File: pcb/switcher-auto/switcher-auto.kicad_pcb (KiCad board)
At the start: 4 copper layers, 160 x 110 mm, 42 parts, among them J1 MD-90SM, J10 MD-90SM, J11 MD-90SM, J12 MD-90SM, J13 MD-90SM, J14 MD-90SM, J15 Conn_02x22_Top_Bottom, J2 Conn_02x22_Top_Bottom, J3 Conn_02x22_Top_Bottom, J4 Conn_02x22_Top_Bottom, SW1 SW_Push, SW2 SW_Push, U1 CD74HC4067SM96, U2 CD74HC4067SM96, U3 CD74HC4067SM96, U4 CD74HC4067SM96, U5 CD74HC4067SM96, U6 CD74HC4067SM96, U7 CD74HC4067SM96

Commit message: Add notes for fab
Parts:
- added H5: MountingHole, MountingHole:MountingHole_2.5mm, F.Cu at (75.0, 37.0)
- renumbered H1 to H10, H2 to H12, H3 to H13, H4 to H14
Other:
- board size 160 x 110 mm -> 160 x 109 mm
- board text added: "PANEL A"
- board text added: "PANEL B"

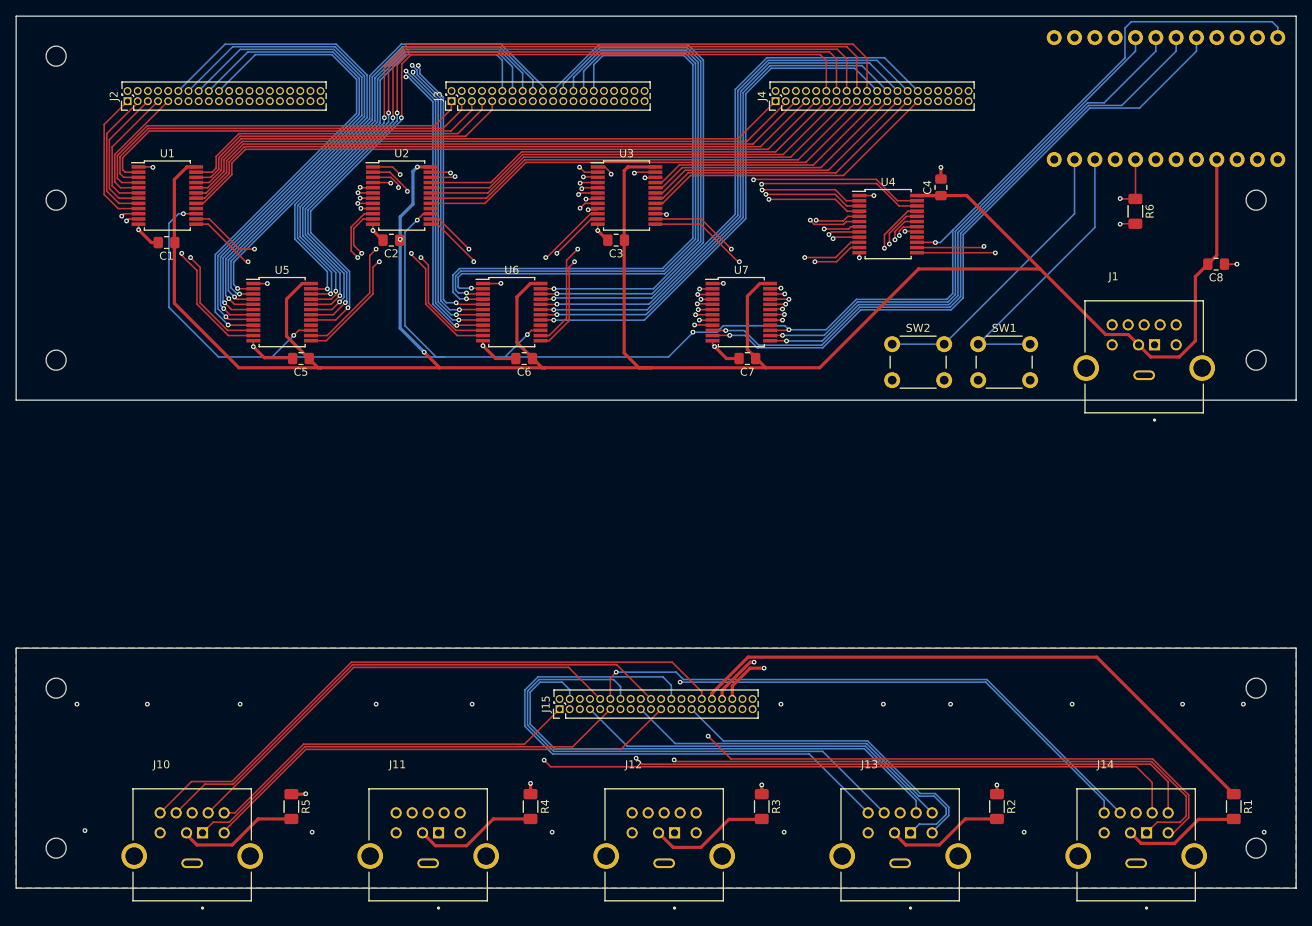
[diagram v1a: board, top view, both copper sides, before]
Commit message: mounting holes should be M3
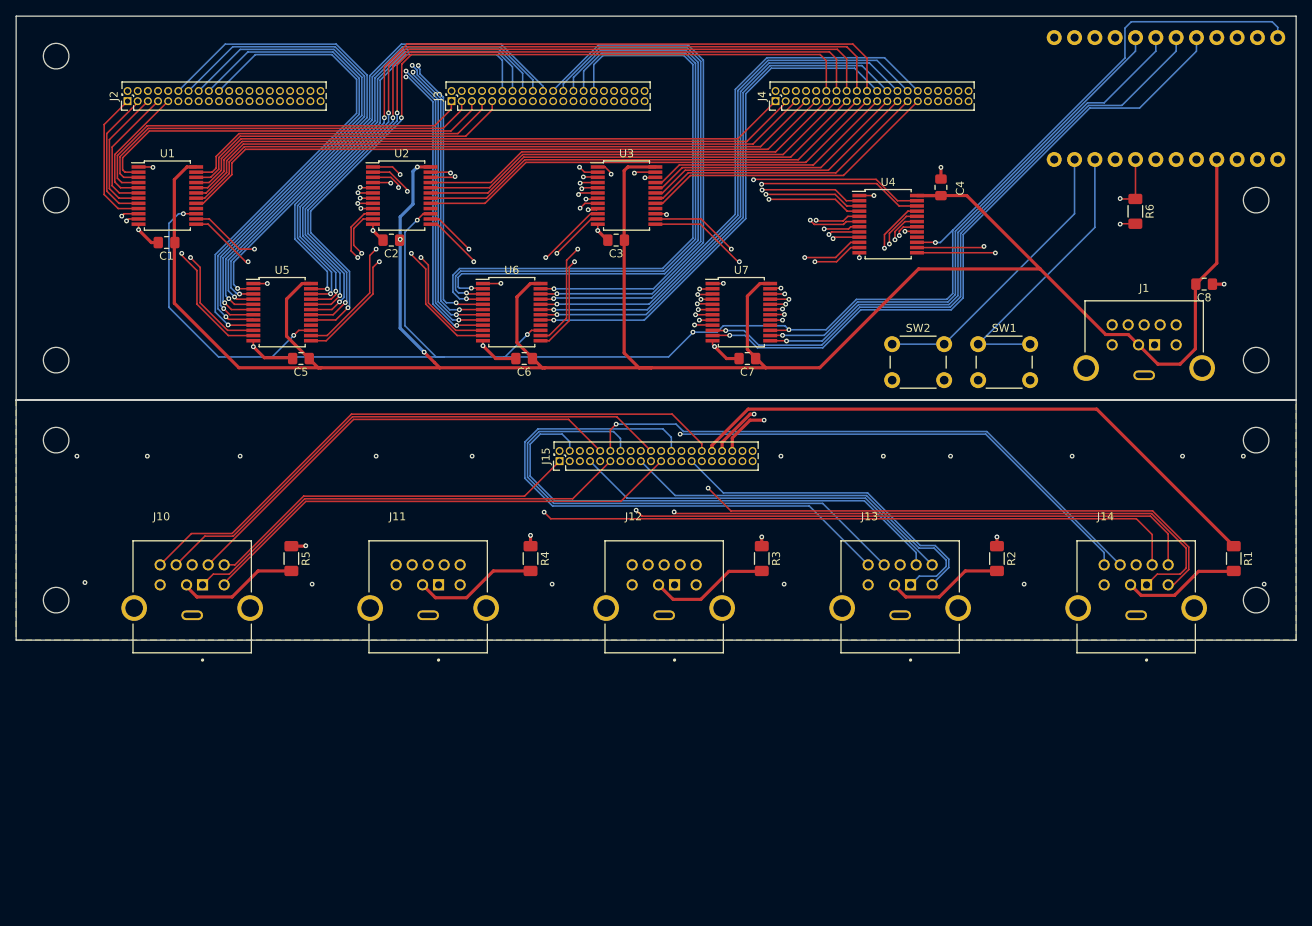
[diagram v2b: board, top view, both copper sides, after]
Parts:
- H1, H10, H12, H13, H14, H2, H3, H4, H5: footprint MountingHole:MountingHole_2.5mm -> MountingHole:MountingHole_3.2mm_M3
- moved R1 31.0 mm to (222.2, 99.8)
- moved R2 31.0 mm to (192.6, 99.8)
- moved R3 31.0 mm to (163.2, 99.8)
- moved R4 31.0 mm to (134.3, 99.8)
- moved R5 31.0 mm to (104.4, 99.8)
- moved H10 31.0 mm to (75.0, 85.0)
- moved H12 31.0 mm to (75.0, 105.0)
- moved H13 31.0 mm to (225.0, 85.0)
- moved H14 31.0 mm to (225.0, 105.0)
- moved J10 31.0 mm to (92.0, 106.9)
- moved J11 31.0 mm to (121.5, 106.9)
- moved J12 31.0 mm to (151.0, 106.9)
- moved J13 31.0 mm to (180.5, 106.9)
- moved J14 31.0 mm to (210.0, 106.9)
- moved J15 31.0 mm to (137.9, 87.6)
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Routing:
- net /VCC: track 309.0 -> 310.3 mm
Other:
- board size 160 x 109 mm -> 160 x 78 mm
- board text added: "DESIGN A"
- board text added: "DESIGN B"
- board text added: "V-Score or cut on this line"
- board text removed: "PANEL A"
- board text removed: "PANEL B"

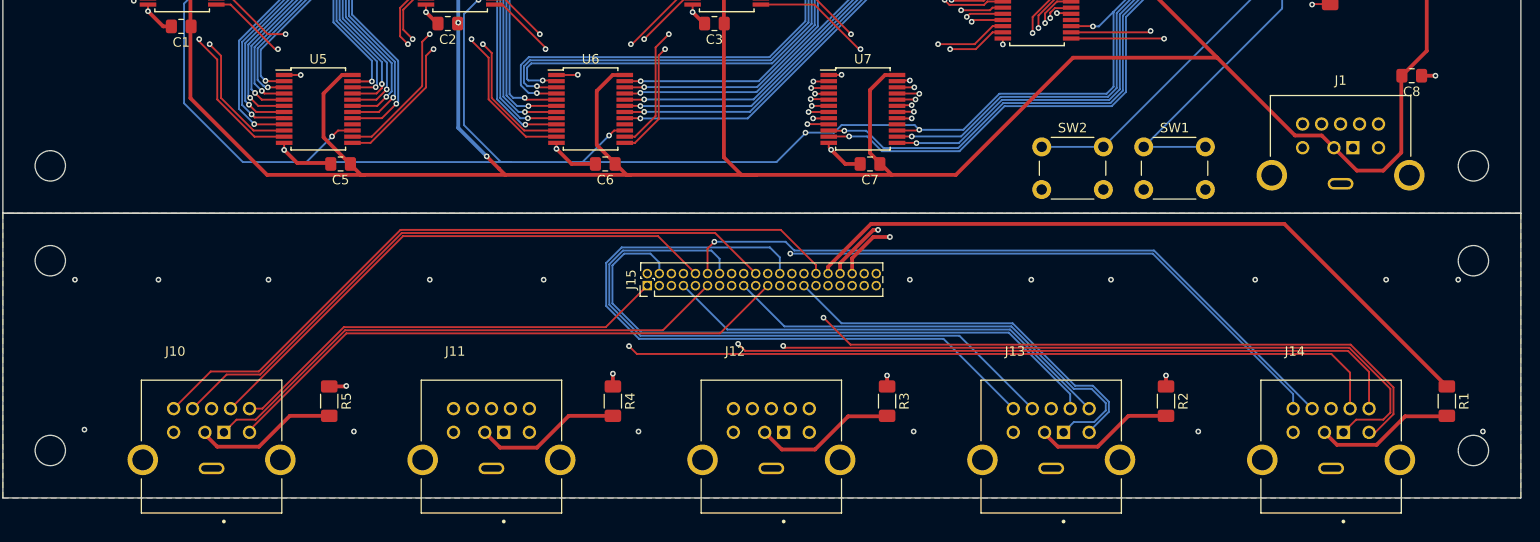
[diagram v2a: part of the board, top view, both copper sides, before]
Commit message: Remove silkscreens, passing DRC
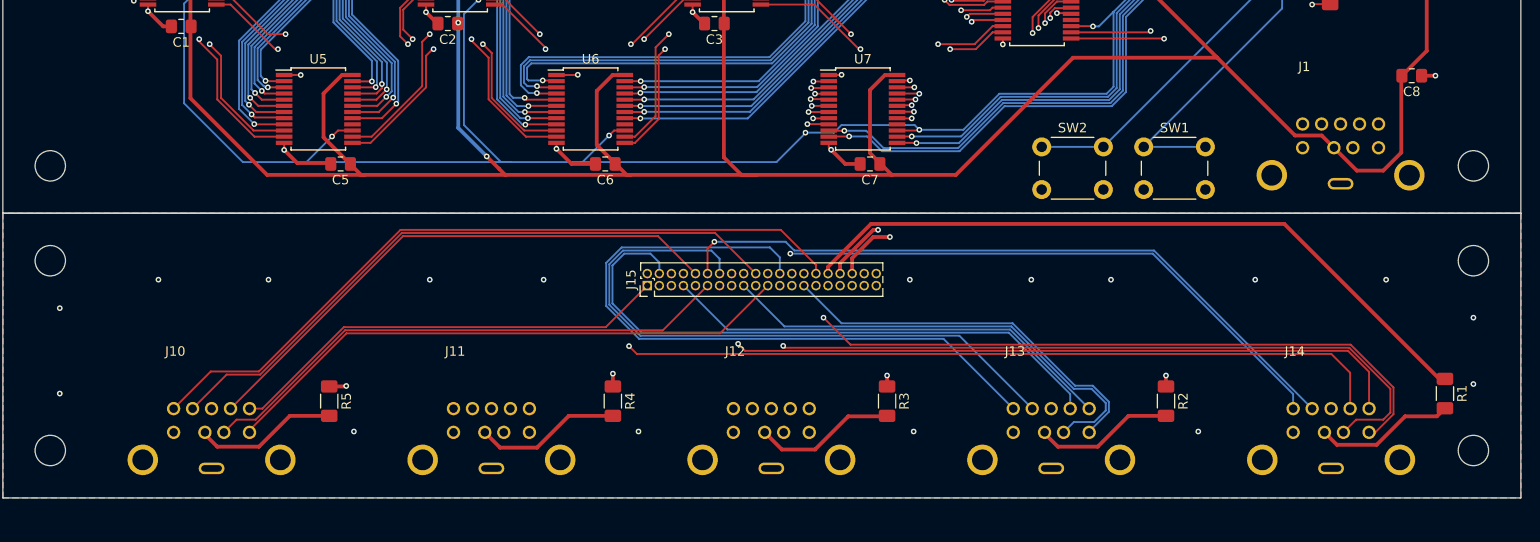
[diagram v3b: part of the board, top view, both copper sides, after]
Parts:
- moved R1 0.82 mm to (222.0, 99.0)
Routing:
- net Net-(J15-Pin_25): track 74.9 -> 74.4 mm

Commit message: WIP
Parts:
- R1, R2, R3, R4, R5, R6: footprint Resistor_SMD:R_1206_3216Metric_Pad1.30x1.75mm_HandSolder -> Resistor_SMD:R_0805_2012Metric_Pad1.20x1.40mm_HandSolder
- U1, U2, U3, U4, U5, U6, U7: footprint Package_SO:SSOP-24_5.3x8.2mm_P0.65mm -> Package_SO:SOIC-24W_7.5x15.4mm_P1.27mm
- moved H10 300.8 mm to (31.1, 382.6)
- moved H12 300.8 mm to (31.1, 402.6)
- moved H13 300.8 mm to (181.1, 382.6)
- moved H14 300.8 mm to (181.1, 402.6)
- moved J10 300.8 mm to (48.1, 404.5)
- moved J11 300.8 mm to (77.6, 404.5)
- moved J12 300.8 mm to (107.1, 404.5)
- moved J13 300.8 mm to (136.6, 404.5)
- moved J14 300.8 mm to (166.1, 404.5)
- moved J15 300.8 mm to (94.0, 385.2)
- moved R1 300.8 mm to (178.1, 396.6)
- moved R2 300.8 mm to (148.7, 397.4)
- moved R3 300.8 mm to (119.3, 397.4)
- moved R4 300.8 mm to (90.4, 397.4)
- moved R5 300.8 mm to (60.5, 397.4)
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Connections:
- U7 pad 10: /R0 -> /S0
- U7 pad 11: /R1 -> /S1
- U7 pad 13: /R3 -> /S3
- U7 pad 14: /R2 -> /S2
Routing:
- net /VCC: track 310.3 -> 0.00 mm, vias 3 -> 0
- net /EN: track 241.7 -> 0.00 mm, vias 8 -> 0
- net /S0: track 202.5 -> 0.00 mm, vias 6 -> 0
- net /S1: track 197.4 -> 0.00 mm, vias 6 -> 0
- net /S2: track 187.6 -> 0.00 mm, vias 6 -> 0
- net /S3: track 176.6 -> 0.00 mm, vias 6 -> 0
- net /SEL_RVID: track 160.6 -> 0.00 mm, vias 1 -> 0
- net /SEL_LAUD: track 119.3 -> 0.00 mm, vias 1 -> 0
- net /SEL_BVID: track 114.6 -> 0.00 mm, vias 1 -> 0
- net /10_LAUD: track 104.4 -> 0.00 mm, vias 2 -> 0
- net /11_LAUD: track 103.5 -> 0.00 mm, vias 2 -> 0
- net /12_LAUD: track 102.4 -> 0.00 mm, vias 2 -> 0
- net /13_LAUD: track 101.3 -> 0.00 mm, vias 2 -> 0
- net /14_LAUD: track 100.2 -> 0.00 mm, vias 2 -> 0
- net /SEL_GVID: track 98.5 -> 0.00 mm, vias 1 -> 0
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- removed copper zone on B.Cu, net /Daughterboard/0_GND
- removed copper zone on F.Cu, net /Daughterboard/0_GND
- removed copper zone on In2.Cu, net GND
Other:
- board size 160 x 78 mm -> 160 x 372.6 mm

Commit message: Finishing routing
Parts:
- removed H10, H12, H13, H14, H3, H4: MountingHole, MountingHole:MountingHole_3.2mm_M3
- added A1: TSOP38238, REB-IR:XDCR_TSOP38238, F.Cu at (129.3, 45.5)
- added H2: MountingHole, MountingHole:MountingHole_3.2mm_M3, F.Cu at (65.0, 155.0)
- added H2: MountingHole, MountingHole:MountingHole_3.2mm_M3, F.Cu at (155.0, 155.0)
- moved R5 252.5 mm to (138.2, 157.1)
- moved R4 245.5 mm to (140.9, 157.1)
- moved R3 241.5 mm to (143.5, 157.1)
- moved R1 241.3 mm to (148.9, 157.1)
- moved R2 240.3 mm to (146.2, 157.1)
- moved J10 230.5 mm to (70.0, 175.0)
- moved J14 230.1 mm to (150.0, 175.0)
- moved J11 229.8 mm to (90.0, 175.0)
- moved J13 229.6 mm to (130.0, 175.0)
- moved J12 229.5 mm to (110.0, 175.0)
- moved J15 227.5 mm to (97.9, 157.7)
- moved C8 125.7 mm to (89.0, 122.0)
- moved H1 98.4 mm to (156.0, 46.0), turned to 90 degrees
- moved C4 62.4 mm to (154.1, 59.3)
- moved H2 51.7 mm to (64.0, 127.0), turned to 90 degrees
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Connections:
- B1 pad 1: /EN -> Net-(A1-OUT)
- U1 pad 15: /EN -> GND
- U2 pad 15: /EN -> GND
- U3 pad 15: /EN -> GND
- U4 pad 15: /EN -> GND
- U5 pad 15: /EN -> GND
- U6 pad 15: /EN -> GND
- U7 pad 15: /EN -> GND
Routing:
- net /VCC: track 0.00 -> 367.0 mm, vias 0 -> 8
- net /S3: track 0.00 -> 193.8 mm, vias 0 -> 3
- net /S0: track 0.00 -> 191.1 mm, vias 0 -> 2
- net /S1: track 0.00 -> 187.0 mm, vias 0 -> 3
- net /S2: track 0.00 -> 184.8 mm, vias 0 -> 3
- net /10_LAUD: track 0.00 -> 107.3 mm, vias 0 -> 2
- net /11_LAUD: track 0.00 -> 106.1 mm, vias 0 -> 2
- net /12_LAUD: track 0.00 -> 105.2 mm, vias 0 -> 2
- net /13_LAUD: track 0.00 -> 104.6 mm, vias 0 -> 2
- net /14_LAUD: track 0.00 -> 103.6 mm, vias 0 -> 2
- net /SEL_CVID: track 0.00 -> 103.1 mm, vias 0 -> 2
- net /Daughterboard/0_VCC: track 0.00 -> 93.4 mm, vias 0 -> 1
- net /10_RAUD: track 0.00 -> 93.2 mm, vias 0 -> 1
- net Net-(A1-OUT): track 0.00 -> 92.8 mm
- net /11_RAUD: track 0.00 -> 92.1 mm, vias 0 -> 1
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- added copper zone on In2.Cu, net /Daughterboard/0_GND
- added copper zone on In2.Cu, net GND
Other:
- board size 160 x 372.6 mm -> 100 x 138 mm
- board text added: "IR Sensor"
- board text removed: "DESIGN A"
- board text removed: "DESIGN B"
- board text removed: "V-Score or cut on this line"

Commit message: Passing DRC
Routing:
- net /VCC: track 367.0 -> 379.5 mm
- net /Daughterboard/3_VCC: track 26.7 -> 25.9 mm, vias 0 -> 1
- net /S3: vias 3 -> 2
- net /S2: vias 3 -> 2
- net /9_CVID: vias 3 -> 2
- net /1_BVID: vias 3 -> 2
- net /0_BVID: vias 3 -> 2

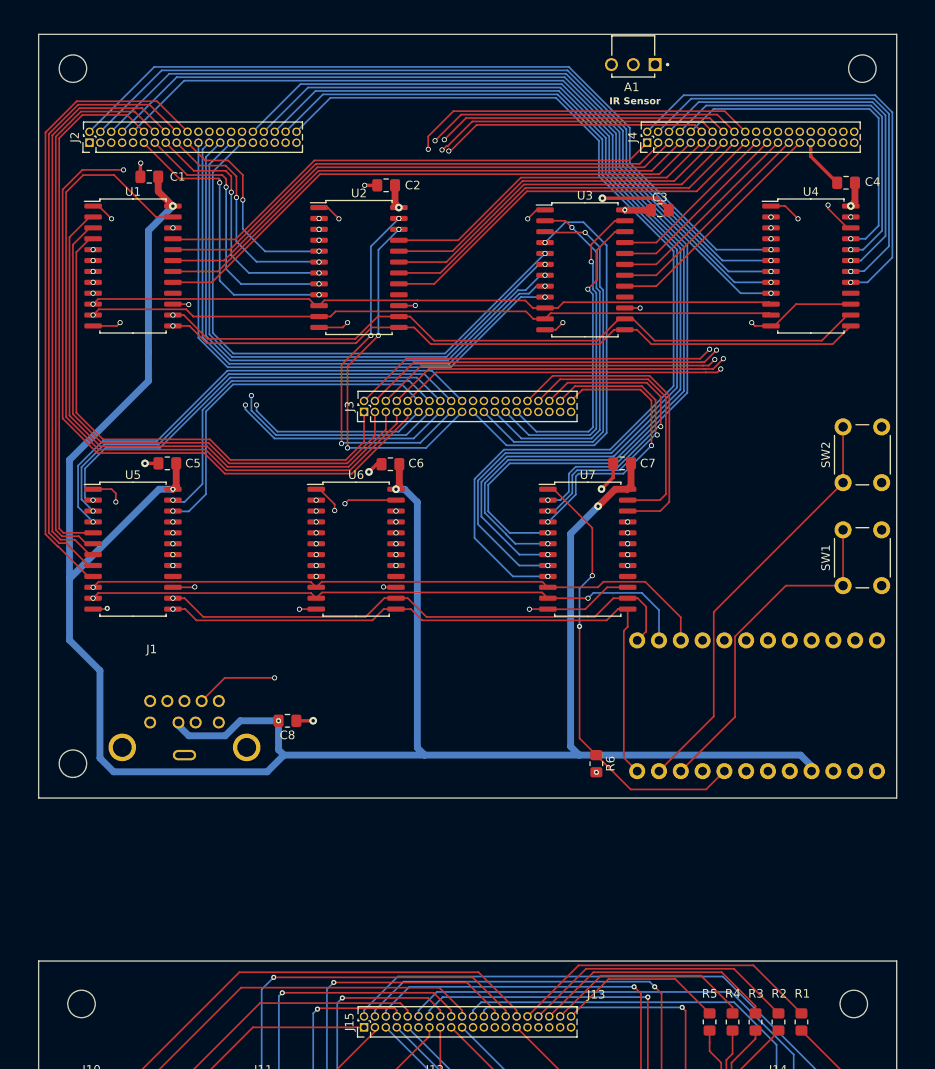
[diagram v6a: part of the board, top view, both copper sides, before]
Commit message: VCC pour
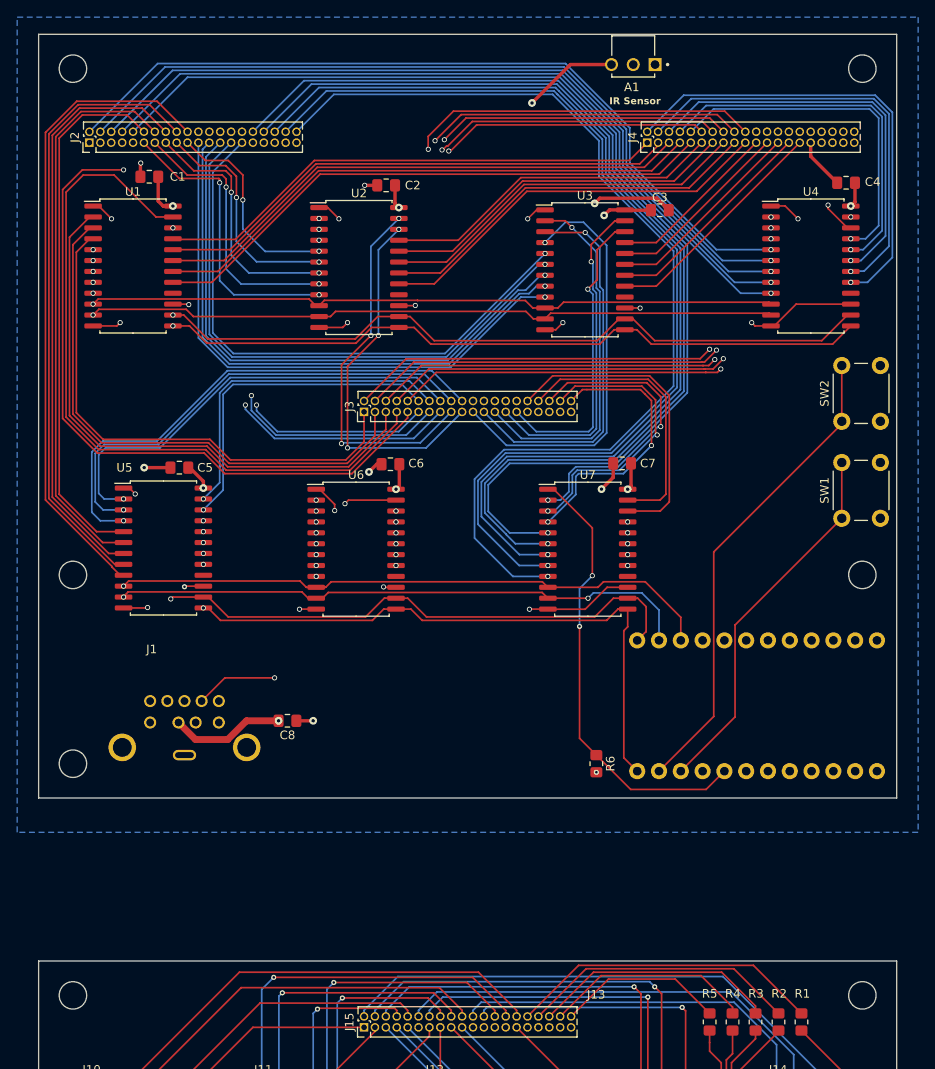
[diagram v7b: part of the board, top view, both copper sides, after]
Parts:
- added H2: MountingHole, MountingHole:MountingHole_3.2mm_M3, F.Cu at (156.0, 105.0)
- added H2: MountingHole, MountingHole:MountingHole_3.2mm_M3, F.Cu at (64.0, 105.0)
- moved SW1 7.85 mm to (153.6, 98.4)
- moved SW2 7.15 mm to (153.6, 87.1)
- moved U5 3.55 mm to (74.5, 101.9)
- moved C5 1.49 mm to (76.4, 92.5)
- moved H2 1.41 mm to (64.0, 154.0)
- moved H2 1.41 mm to (156.0, 154.0)
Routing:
- net /VCC: track 379.5 -> 50.1 mm, vias 8 -> 9
- net Net-(B1-11(MOSI)): track 49.0 -> 56.1 mm
- net /S0: track 191.1 -> 185.6 mm
- net Net-(B1-12(MISO)): track 39.9 -> 43.7 mm
- net /S1: track 187.0 -> 183.1 mm
- net /13_LAUD: track 104.6 -> 100.8 mm
- net /12_LAUD: track 105.2 -> 101.6 mm
- net /10_LAUD: track 107.3 -> 103.7 mm
- net /14_LAUD: track 103.6 -> 100.0 mm
- net /11_LAUD: track 106.1 -> 102.6 mm
- net GND: track 74.1 -> 77.6 mm
- net /9_LAUD: track 41.2 -> 38.5 mm
- net /8_LAUD: track 41.8 -> 39.1 mm
- net /S3: track 193.8 -> 191.3 mm
- net /SEL_LAUD: track 29.5 -> 27.3 mm
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- added copper zone on B.Cu, net /VCC
